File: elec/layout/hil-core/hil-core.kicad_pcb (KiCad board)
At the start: 4 copper layers, 113 parts, among them U4 10µH ±20%

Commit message: update LED gpio pin
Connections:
- net CC2 renamed B5
- net SW renamed buck_5v-cathode
- net controller.cm5-pins[47] renamed pins[47]
- net controller.cm5-pins[87] renamed controller.cm5-pins[89]
- net controller.cm5-pins[87]-1 renamed pins[87]
- net pins[23] renamed controller.cm5.hdi_b-pins[23]
- net pins[40] renamed controller.cm5.hdi_b-pins[40]
- net pins[53] renamed controller.cm5-pins[53]-1
- net pins[89] renamed controller.cm5-pins[89]-1
- net usb_connector.connector-B2 renamed B2
- net usbpd.usb_connector-B2 renamed SSTXP2
- C10 pad 1: hv-8 -> hv-7
- C11 pad 1: hv-8 -> hv-7
- C12 pad 1: hv -> hv-1
- C15 pad 1: hv-8 -> hv-7
- C16 pad 1: hv-1 -> hv
- C17 pad 1: hv-6 -> hv-9
- C18 pad 1: hv-6 -> hv-9
- C2 pad 1: hv-7 -> hv-4
- C20 pad 1: hv -> hv-1
- C21 pad 1: hv -> hv-1
- C26 pad 1: hv-2 -> hv-5
- C26 pad 2: gnd-1 -> gnd
- C27 pad 1: hv-2 -> hv-5
- C27 pad 2: gnd-1 -> gnd
- C28 pad 2: gnd-1 -> gnd
- C29 pad 2: gnd-1 -> gnd
- C3 pad 1: hv-7 -> hv-4
- C30 pad 1: hv -> hv-1
- C31 pad 1: hv -> hv-1
- C32 pad 1: hv -> hv-1
- C33 pad 1: hv -> hv-1
- C34 pad 1: hv -> hv-1
- C35 pad 1: hv -> hv-1
- C36 pad 1: hv -> hv-1
- C37 pad 1: hv -> hv-1
- C4 pad 1: hv-4 -> hv-6
- C40 pad 1: hv-8 -> hv-7
- C41 pad 1: hv-5 -> hv-2
- C42 pad 1: hv-5 -> hv-2
- C43 pad 1: hv-5 -> hv-2
- C44 pad 1: hv-5 -> hv-2
- C45 pad 1: hv-5 -> hv-2
- C5 pad 1: hv-4 -> hv-6
- C6 pad 1: hv-4 -> hv-6
- C9 pad 1: hv-4 -> hv-6
- CN1 pad 12: controller.cm5-line-4 -> controller.cm5-pins[23]
- CN1 pad 13: pins[25] -> controller.cm5-line-3
- CN1 pad 14: controller-line-3 -> controller-line
- CN1 pad 15: controller.cm5-line -> controller.cm5-line-5
- CN1 pad 18: controller-line-12 -> controller-line-4
- CN1 pad 19: controller-line-11 -> controller-line-29
- CN1 pad 2: controller-line-24 -> controller-line-9
- CN1 pad 20: controller-line-9 -> controller-line-8
- CN1 pad 22: controller-line-10 -> controller-line-24
- CN1 pad 23: line-4 -> line-10
- CN1 pad 24: controller.cm5-pins[47]-1 -> controller.cm5-line-1
- CN1 pad 25: line -> line-9
- CN1 pad 27: controller.cm5-line-1 -> controller.cm5-pins[53]
- CN1 pad 28: controller-line-26 -> controller-line-3
- CN1 pad 29: controller-line-16 -> controller-line-2
- CN1 pad 3: controller-line-4 -> controller-line-21
- CN1 pad 39: hv-9 -> hv-8
- CN1 pad 42: hv-9 -> hv-8
- CN1 pad 43: hv-9 -> hv-8
- CN1 pad 5: controller-line-2 -> controller-line-10
- CN1 pad 57: hv-8 -> hv-7
- CN1 pad 58: hv-8 -> hv-7
- CN1 pad 59: hv-8 -> hv-7
- CN1 pad 6: controller-line-21 -> controller-line-20
- CN1 pad 60: hv-8 -> hv-7
- CN1 pad 61: hv-8 -> hv-7
- CN1 pad 62: hv-8 -> hv-7
- CN1 pad 73: line-6 -> line-1
- CN1 pad 75: line-10 -> line-8
- CN1 pad 76: controller.cm5-line-3 -> controller.cm5-line-4
- CN1 pad 77: line-3 -> line-11
- CN1 pad 78: controller.cm5-line-5 -> controller.cm5-line
- CN1 pad 80: controller.cm5-line-2 -> controller.cm5-pins[40]
- CN1 pad 81: controller-line -> controller-line-6
- CN1 pad 82: controller-line-7 -> controller-line-31
- CN1 pad 83: controller-line-5 -> controller-line-19
- CN1 pad 85: controller-line-8 -> controller-line-7
- CN1 pad 86: line-9 -> line-6
- CN1 pad 88: pins[24] -> controller.cm5-line-2
- CN1 pad 92: controller-line-28 -> controller-line-14
- CN1 pad 93: controller-line-19 -> controller-line-25
- CN1 pad 95: controller-line-27 -> controller-line-1
- CN1 pad 96: controller-line-15 -> controller-line-11
- CN1 pad 99: controller-line-31 -> controller-line-12
- CN2 pad 15: controller-line-23 -> controller-line-26
- CN2 pad 17: controller-line-17 -> controller-line-27
- CN2 pad 18: controller-line-20 -> controller-line-22
- CN2 pad 20: controller-line-1 -> controller-line-18
- CN2 pad 21: controller-line-6 -> controller-line-23
- CN2 pad 65: controller-line-22 -> controller-line-17
- CN2 pad 66: controller-line-25 -> controller-line-13
- CN2 pad 68: controller-line-13 -> controller-line-16
- CN2 pad 69: controller-line-18 -> controller-line-5
- CN2 pad 71: controller-line-29 -> controller-line-15
- CN2 pad 72: controller-line-14 -> controller-line-28
- CN2 pad 98: line-2 -> line
- CN2 pad 99: line-1 -> line-4
- D1 pad 1: hv-4 -> hv-6
- D10 pad 2: usb_hub-line-2 -> usb_hub-line
- D10 pad 3: usb_hub-line-1 -> usb_hub-line-4
- D10 pad 4: hv-5 -> hv-2
- D11 pad 2: usb_hub-line -> usb_hub-line-1
- D11 pad 3: usb_hub-line-4 -> usb_hub-line-2
- D11 pad 4: hv-5 -> hv-2
- D12 pad 2: line-8 -> line-7
- D12 pad 3: line-7 -> line-3
- D12 pad 4: hv-5 -> hv-2
- D2 pad 1: controller.cm5-cathode-1 -> controller.cm5-cathode
- D2 pad 2: hv-9 -> hv-8
- D3 pad 1: controller.cm5-cathode -> controller.cm5-cathode-1
- D3 pad 2: hv-9 -> hv-8
- D4 pad 1: usbpd-line-5 -> usbpd-line-2
- D4 pad 2: usbpd-line-3 -> usbpd-line-4
- D6 pad 1: hv-7 -> hv-4
- D7 pad 1: gnd-1 -> gnd
- D7 pad 2: line-11 -> line-5
- D7 pad 3: line-5 -> line-2
- D8 pad 2: line-11 -> line-5
- D8 pad 3: line-5 -> line-2
- D8 pad 4: hv-5 -> hv-2
- D9 pad 2: line-1 -> line-4
- D9 pad 3: line-2 -> line
- D9 pad 4: hv-5 -> hv-2
- L1 pad 1: hv-7 -> hv-4
- OLED1 pad 10: line-3 -> line-11
- OLED1 pad 11: line-4 -> line-10
- OLED1 pad 14: hv-6 -> hv-9
- OLED1 pad 5: hv-1 -> hv
- OLED1 pad 8: hv -> hv-1
- Q1 pad 5: hv-7 -> hv-4
- Q1 pad 6: hv-7 -> hv-4
- Q1 pad 7: hv-7 -> hv-4
- Q1 pad 8: hv-7 -> hv-4
- Q1 pad 9: hv-7 -> hv-4
- R10 pad 1: hv-9 -> hv-8
- R10 pad 2: controller.rj45-anode -> controller.rj45-anode-1
- R12 pad 1: hv -> hv-1
- R15 pad 1: hv-1 -> hv
- R17 pad 1: usbpd-line-4 -> usbpd-line-1
- R18 pad 1: usbpd-line -> usbpd-line-3
- R2 pad 1: hv-4 -> hv-6
- R20 pad 2: hv-7 -> hv-4
- R23 pad 2: gnd-1 -> gnd
- R25 pad 1: usb_hub.hub-line -> usb_hub.hub-line-1
- R26 pad 1: usb_hub.hub-line-1 -> usb_hub.hub-line
- R6 pad 1: hv-8 -> hv-7
- R7 pad 1: controller.cm5-cathode-1 -> controller.cm5-cathode
- R8 pad 1: controller.cm5-cathode -> controller.cm5-cathode-1
- R9 pad 1: hv-9 -> hv-8
- R9 pad 2: controller.rj45-anode-1 -> controller.rj45-anode
- RJ1 pad 11: controller.rj45-anode-1 -> controller.rj45-anode
- RJ1 pad 12: controller-line-19 -> controller-line-25
- RJ1 pad 13: controller-line-28 -> controller-line-14
- RJ1 pad 14: controller.rj45-anode -> controller.rj45-anode-1
- RJ1 pad P2: controller-line-21 -> controller-line-20
- RJ1 pad P3: controller-line-2 -> controller-line-10
- RJ1 pad P4: controller-line-24 -> controller-line-9
- RJ1 pad P5: controller-line-27 -> controller-line-1
- RJ1 pad P6: controller-line-15 -> controller-line-11
- RJ1 pad P7: controller-line-4 -> controller-line-21
- RJ1 pad P8: controller-line-31 -> controller-line-12
- U1 pad 2: hv-7 -> hv-4
- U1 pad 3: hv-7 -> hv-4
- U10 pad 1: hv-8 -> hv-7
- U10 pad 3: hv-8 -> hv-7
- U10 pad 5: hv -> hv-1
- U11 pad 1: hv-8 -> hv-7
- U11 pad 3: hv-8 -> hv-7
- U11 pad 5: hv-1 -> hv
- U12 pad 1: usbpd-line-5 -> usbpd-line-2
- U12 pad 2: usbpd-line-5 -> usbpd-line-2
- U12 pad 4: usbpd-line-3 -> usbpd-line-4
- U12 pad 5: usbpd-line-3 -> usbpd-line-4
- U12 pad 7: usbpd-line-4 -> usbpd-line-1
- U12 pad 8: usbpd-line -> usbpd-line-3
- U13 pad 1: usb_uart-line-3 -> usb_uart-line
- U13 pad 2: usb_uart-line -> usb_uart-line-3
- U13 pad 23: line -> line-9
- U13 pad 24: line-9 -> line-6
- U13 pad 25: line-6 -> line-1
- U13 pad 26: line-10 -> line-8
- U13 pad 29: gnd-1 -> gnd
- U13 pad 3: gnd-1 -> gnd
- U13 pad 4: line-5 -> line-2
- U13 pad 5: line-11 -> line-5
- U13 pad 7: hv-2 -> hv-5
- U14 pad 1: line-11 -> line-5
- U14 pad 10: hv -> hv-1
- U14 pad 15: hv -> hv-1
- U14 pad 2: line-5 -> line-2
- U14 pad 22: usb_hub.hub-line-1 -> usb_hub.hub-line
- U14 pad 23: hv -> hv-1
- U14 pad 24: usb_hub.hub-line -> usb_hub.hub-line-1
- U14 pad 27: hv -> hv-1
- U14 pad 29: hv -> hv-1
- U14 pad 3: line-1 -> line-4
- U14 pad 30: line-8 -> line-7
- U14 pad 31: line-7 -> line-3
- U14 pad 36: hv -> hv-1
- U14 pad 4: line-2 -> line
- U14 pad 5: hv -> hv-1
- U14 pad 6: usb_hub-line-2 -> usb_hub-line
- U14 pad 7: usb_hub-line-1 -> usb_hub-line-4
- U14 pad 8: usb_hub-line -> usb_hub-line-1
- U14 pad 9: usb_hub-line-4 -> usb_hub-line-2
- U15 pad 1: hv-8 -> hv-7
- U15 pad 6: hv-5 -> hv-2
- U3 pad 4: hv-4 -> hv-6
- U3 pad 5: hv-4 -> hv-6
- U4 pad 2: hv-8 -> hv-7
- U5 pad 5: hv-9 -> hv-8
- USB1 pad A5: usbpd-line-5 -> usbpd-line-2
- USB1 pad A6: usbpd-line-1 -> usbpd-line
- USB1 pad A7: usbpd-line-2 -> usbpd-line-5
- USB1 pad B5: usbpd-line-3 -> usbpd-line-4
- USB1 pad B6: usbpd-line-1 -> usbpd-line
- USB1 pad B7: usbpd-line-2 -> usbpd-line-5
- USB2 pad A6: line-7 -> line-3
- USB2 pad A7: line-8 -> line-7
- USB2 pad B6: line-7 -> line-3
- USB2 pad B7: line-8 -> line-7
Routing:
- net (no net): track 207.6 -> 330.8 mm, vias 8 -> 74
- net gnd-1: track 123.1 -> 0.00 mm, vias 66 -> 0
- net line-8: track 58.7 -> 0.00 mm, vias 3 -> 0
- net line-3: track 0.00 -> 53.8 mm, vias 0 -> 2
- net line-4: track 0.00 -> 38.7 mm, vias 0 -> 2
- net line-1: track 38.7 -> 0.00 mm, vias 2 -> 0
- net line: track 0.00 -> 38.1 mm, vias 0 -> 2
- net hv-5: track 40.8 -> 3.36 mm, vias 6 -> 0
- net hv-2: track 3.36 -> 40.8 mm, vias 0 -> 6
- net controller-line-28: track 29.5 -> 0.00 mm, vias 1 -> 0
- net controller-line-14: track 0.00 -> 29.5 mm, vias 0 -> 1
- net controller-line-25: track 0.00 -> 24.6 mm, vias 0 -> 1
- net controller-line-19: track 24.6 -> 0.00 mm, vias 1 -> 0
- net line-2: track 38.1 -> 14.9 mm
- net controller-line-2: track 19.6 -> 0.00 mm, vias 1 -> 0
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- added copper zone on F.Cu, net hv-6
- removed copper zone on F.Cu, net hv-8

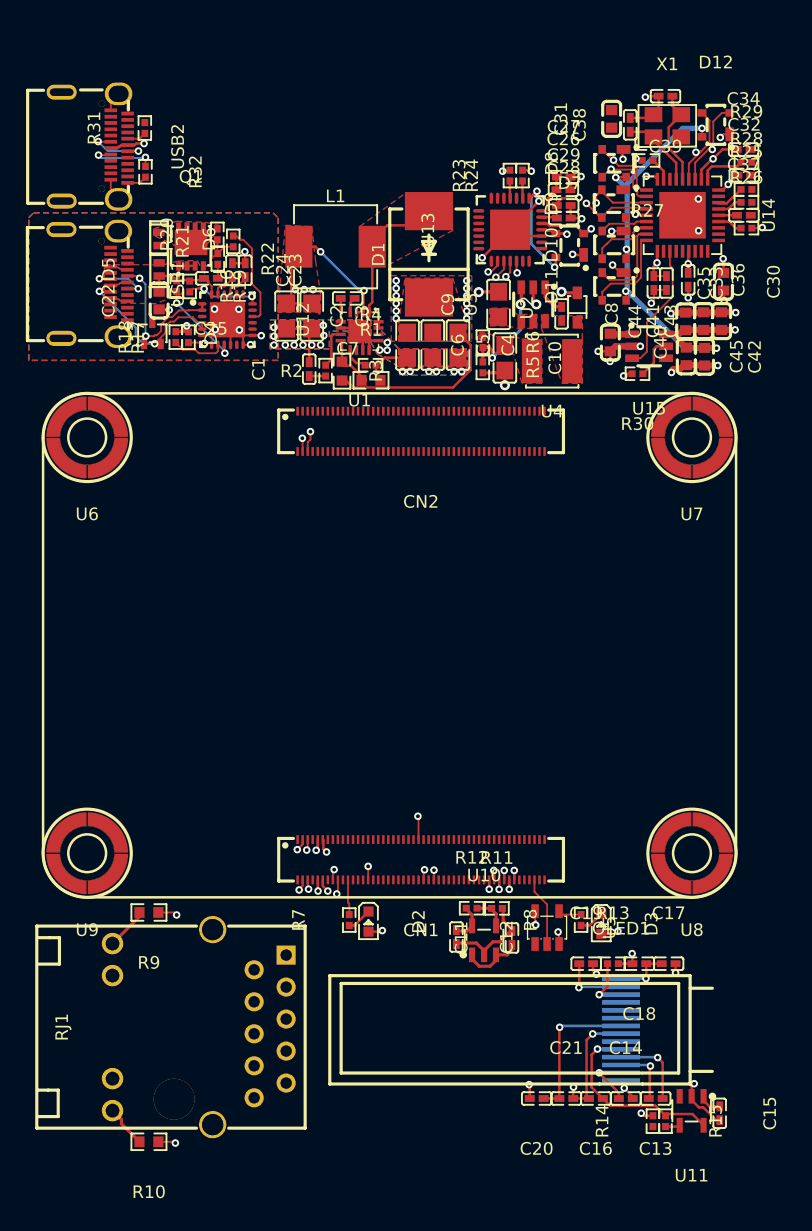
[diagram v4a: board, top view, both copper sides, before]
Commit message: add power button and boot button, fix CAN layout
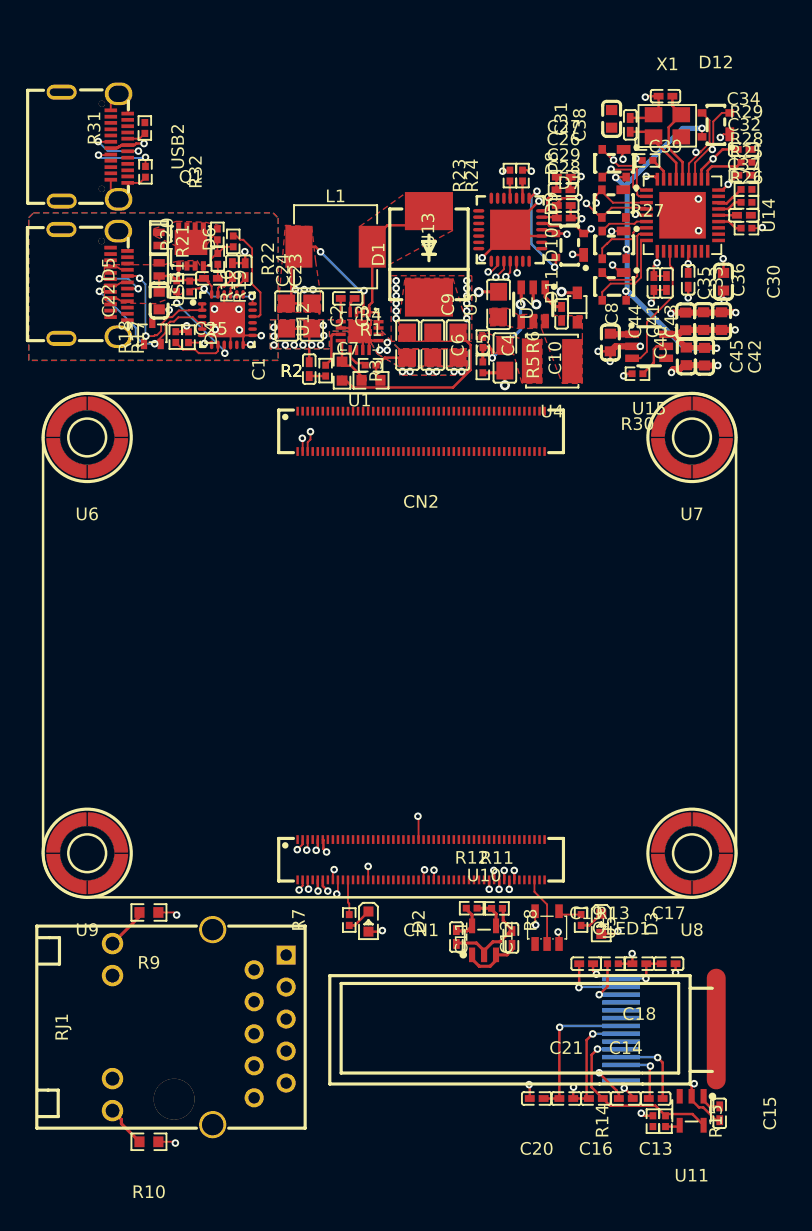
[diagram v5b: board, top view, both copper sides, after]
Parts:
- R11: value 10kΩ ±1% 62.5mW -> 5.6kΩ ±1% 62.5mW
- R6: value 10kΩ ±1% 62.5mW -> 47kΩ ±1% 62.5mW
- R7, R8: value 10kΩ ±1% 62.5mW -> 2kΩ ±1% 62.5mW
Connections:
- net B2 renamed usb_connector.connector-B2
- net SSTXP2 renamed usbpd.usb_connector-B2
- net buck_5v-cathode renamed SW
- net controller.cm5-pins[53]-1 renamed pins[53]
- net controller.cm5-pins[89] renamed controller.cm5-pins[87]
- net controller.cm5-pins[89]-1 renamed pins[89]
- net controller.cm5.hdi_b-pins[23] renamed pins[23]
- net controller.cm5.hdi_b-pins[26] renamed pins[26]
- net pins[44] renamed controller.cm5-pins[44]-1
- net pins[48] renamed controller.cm5-pins[48]-1
- net pins[87] renamed controller.cm5-pins[87]-1
- net usb_connector.connector-A2 renamed SSTXP1
- net usb_connector.connector-A3 renamed SSTXN1
- net usb_connector.connector-A8 renamed SBU1
- net usb_connector.connector-B10 renamed SSRXN1
- net usb_connector.connector-B11 renamed SSRXP1
- net usbpd.usb_connector-A2 renamed A2
- net usbpd.usb_connector-A3 renamed A3
- net usbpd.usb_connector-A8 renamed A8
- net usbpd.usb_connector-B10 renamed B10
- net usbpd.usb_connector-B11 renamed B11
- C10 pad 1: hv-7 -> hv-8
- C11 pad 1: hv-7 -> hv-8
- C12 pad 1: hv-1 -> hv
- C15 pad 1: hv-7 -> hv-8
- C16 pad 1: hv -> hv-1
- C17 pad 1: hv-9 -> hv-4
- C18 pad 1: hv-9 -> hv-4
- C2 pad 1: hv-4 -> hv-2
- C20 pad 1: hv-1 -> hv
- C21 pad 1: hv-1 -> hv
- C26 pad 1: hv-5 -> hv-6
- C27 pad 1: hv-5 -> hv-6
- C28 pad 1: hv-3 -> hv-7
- C29 pad 1: hv-3 -> hv-7
- C3 pad 1: hv-4 -> hv-2
- C30 pad 1: hv-1 -> hv
- C31 pad 1: hv-1 -> hv
- C32 pad 1: hv-1 -> hv
- C33 pad 1: hv-1 -> hv
- C34 pad 1: hv-1 -> hv
- C35 pad 1: hv-1 -> hv
- C36 pad 1: hv-1 -> hv
- C37 pad 1: hv-1 -> hv
- C4 pad 1: hv-6 -> hv-9
- C40 pad 1: hv-7 -> hv-8
- C41 pad 1: hv-2 -> hv-3
- C42 pad 1: hv-2 -> hv-3
- C43 pad 1: hv-2 -> hv-3
- C44 pad 1: hv-2 -> hv-3
- C45 pad 1: hv-2 -> hv-3
- C5 pad 1: hv-6 -> hv-9
- C6 pad 1: hv-6 -> hv-9
- C9 pad 1: hv-6 -> hv-9
- CN1 pad 12: controller.cm5-pins[23] -> controller.cm5-line-3
- CN1 pad 13: controller.cm5-line-3 -> controller.cm5-line-4
- CN1 pad 14: controller-line -> controller-line-8
- CN1 pad 15: controller.cm5-line-5 -> controller-line-27
- CN1 pad 18: controller-line-4 -> controller-line-18
- CN1 pad 19: controller-line-29 -> controller-line-13
- CN1 pad 2: controller-line-9 -> controller-line-3
- CN1 pad 20: controller-line-8 -> controller-line-7
- CN1 pad 22: controller-line-24 -> controller-line-17
- CN1 pad 23: line-10 -> line-11
- CN1 pad 24: controller.cm5-line-1 -> controller.cm5-line
- CN1 pad 25: line-9 -> line-6
- CN1 pad 27: controller.cm5-pins[53] -> controller.cm5-line-5
- CN1 pad 28: controller-line-3 -> controller-line-6
- CN1 pad 3: controller-line-21 -> controller-line-30
- CN1 pad 39: hv-8 -> hv-5
- CN1 pad 42: hv-8 -> hv-5
- CN1 pad 43: hv-8 -> hv-5
- CN1 pad 5: controller-line-10 -> controller-line-25
- CN1 pad 57: hv-7 -> hv-8
- CN1 pad 58: hv-7 -> hv-8
- CN1 pad 59: hv-7 -> hv-8
- CN1 pad 6: controller-line-20 -> controller-line-16
- CN1 pad 60: hv-7 -> hv-8
- CN1 pad 61: hv-7 -> hv-8
- CN1 pad 62: hv-7 -> hv-8
- CN1 pad 73: line-1 -> line-4
- CN1 pad 75: line-8 -> line-2
- CN1 pad 76: controller.cm5-line-4 -> controller.cm5-pins[48]
- CN1 pad 77: line-11 -> line-10
- CN1 pad 78: controller.cm5-line -> controller.cm5-pins[44]
- CN1 pad 81: controller-line-6 -> controller-line-23
- CN1 pad 82: controller-line-31 -> controller-line-4
- CN1 pad 83: controller-line-19 -> controller-line-26
- CN1 pad 85: controller-line-7 -> controller-line-19
- CN1 pad 86: line-6 -> line-7
- CN1 pad 87: controller.cm5-pins[26] -> controller-line-22
- CN1 pad 88: controller.cm5-line-2 -> controller.cm5-line-1
- CN1 pad 92: controller-line-14 -> controller-line-1
- CN1 pad 93: controller-line-25 -> controller-line-15
- CN1 pad 95: controller-line-1 -> controller-line
- CN1 pad 96: controller-line-11 -> controller-line-24
- CN1 pad 98: controller-line-30 -> controller-line-28
- CN1 pad 99: controller-line-12 -> controller-line-32
- CN2 pad 15: controller-line-26 -> controller-line-10
- CN2 pad 17: controller-line-27 -> controller-line-20
- CN2 pad 18: controller-line-22 -> controller-line-31
- CN2 pad 20: controller-line-18 -> controller-line-12
- CN2 pad 21: controller-line-23 -> controller-line-14
- CN2 pad 65: controller-line-17 -> controller-line-11
- CN2 pad 66: controller-line-13 -> controller-line-5
- CN2 pad 68: controller-line-16 -> controller-line-29
- CN2 pad 69: controller-line-5 -> controller-line-9
- CN2 pad 71: controller-line-15 -> controller-line-21
- CN2 pad 72: controller-line-28 -> controller-line-33
- CN2 pad 98: line -> line-1
- CN2 pad 99: line-4 -> line-3
- D1 pad 1: hv-6 -> hv-9
- D10 pad 2: usb_hub-line -> usb_hub-line-2
- D10 pad 4: hv-2 -> hv-3
- D11 pad 2: usb_hub-line-1 -> usb_hub-line
- D11 pad 3: usb_hub-line-2 -> usb_hub-line-1
- D11 pad 4: hv-2 -> hv-3
- D12 pad 2: line-7 -> line-5
- D12 pad 3: line-3 -> line-9
- D12 pad 4: hv-2 -> hv-3
- D2 pad 1: controller.cm5-cathode -> controller.cm5-cathode-1
- D2 pad 2: hv-8 -> hv-5
- D3 pad 1: controller.cm5-cathode-1 -> controller.cm5-cathode
- D3 pad 2: hv-8 -> hv-5
- D4 pad 1: usbpd-line-2 -> usbpd-line-5
- D4 pad 2: usbpd-line-4 -> usbpd-line-2
- D6 pad 1: hv-4 -> hv-2
- D7 pad 2: line-5 -> line-8
- D7 pad 3: line-2 -> line
- D8 pad 2: line-5 -> line-8
- D8 pad 3: line-2 -> line
- D8 pad 4: hv-2 -> hv-3
- D9 pad 2: line-4 -> line-3
- D9 pad 3: line -> line-1
- D9 pad 4: hv-2 -> hv-3
- L1 pad 1: hv-4 -> hv-2
- OLED1 pad 10: line-11 -> line-10
- OLED1 pad 11: line-10 -> line-11
- OLED1 pad 14: hv-9 -> hv-4
- OLED1 pad 5: hv -> hv-1
- OLED1 pad 8: hv-1 -> hv
- Q1 pad 5: hv-4 -> hv-2
- Q1 pad 6: hv-4 -> hv-2
- Q1 pad 7: hv-4 -> hv-2
- Q1 pad 8: hv-4 -> hv-2
- Q1 pad 9: hv-4 -> hv-2
- R10 pad 1: hv-8 -> hv-5
- R12 pad 1: hv-1 -> hv
- R15 pad 1: hv -> hv-1
- R18 pad 1: usbpd-line-3 -> usbpd-line-4
- R2 pad 1: hv-6 -> hv-9
- R20 pad 2: hv-4 -> hv-2
- R24 pad 2: hv-3 -> hv-7
- R25 pad 1: usb_hub.hub-line-1 -> usb_hub.hub-line
- R26 pad 1: usb_hub.hub-line -> usb_hub.hub-line-1
- R6 pad 1: hv-7 -> hv-8
- R7 pad 1: controller.cm5-cathode -> controller.cm5-cathode-1
- R8 pad 1: controller.cm5-cathode-1 -> controller.cm5-cathode
- R8 pad 2: Y -> controller.cm5-line-2
- R9 pad 1: hv-8 -> hv-5
- RJ1 pad 12: controller-line-25 -> controller-line-15
- RJ1 pad 13: controller-line-14 -> controller-line-1
- RJ1 pad P2: controller-line-20 -> controller-line-16
- RJ1 pad P3: controller-line-10 -> controller-line-25
- RJ1 pad P4: controller-line-9 -> controller-line-3
- RJ1 pad P5: controller-line-1 -> controller-line
- RJ1 pad P6: controller-line-11 -> controller-line-24
- RJ1 pad P7: controller-line-21 -> controller-line-30
- RJ1 pad P8: controller-line-12 -> controller-line-32
- RJ1 pad P9: controller-line-30 -> controller-line-28
- U1 pad 2: hv-4 -> hv-2
- U1 pad 3: hv-4 -> hv-2
- U10 pad 1: hv-7 -> hv-8
- U10 pad 3: hv-7 -> hv-8
- U10 pad 5: hv-1 -> hv
- U11 pad 1: hv-7 -> hv-8
- U11 pad 3: hv-7 -> hv-8
- U11 pad 5: hv -> hv-1
- U12 pad 1: usbpd-line-2 -> usbpd-line-5
- U12 pad 2: usbpd-line-2 -> usbpd-line-5
- U12 pad 4: usbpd-line-4 -> usbpd-line-2
- U12 pad 5: usbpd-line-4 -> usbpd-line-2
- U12 pad 8: usbpd-line-3 -> usbpd-line-4
- U13 pad 1: usb_uart-line -> usb_uart-line-2
- U13 pad 2: usb_uart-line-3 -> usb_uart-line
- U13 pad 23: line-9 -> line-6
- U13 pad 24: line-6 -> line-7
- U13 pad 25: line-1 -> line-4
- U13 pad 26: line-8 -> line-2
- U13 pad 27: usb_uart-line-1 -> usb_uart-line-3
- U13 pad 28: usb_uart-line-2 -> usb_uart-line-1
- U13 pad 4: line-2 -> line
- U13 pad 5: line-5 -> line-8
- U13 pad 6: hv-3 -> hv-7
- U13 pad 7: hv-5 -> hv-6
- U14 pad 1: line-5 -> line-8
- U14 pad 10: hv-1 -> hv
- U14 pad 15: hv-1 -> hv
- U14 pad 2: line-2 -> line
- U14 pad 22: usb_hub.hub-line -> usb_hub.hub-line-1
- U14 pad 23: hv-1 -> hv
- U14 pad 24: usb_hub.hub-line-1 -> usb_hub.hub-line
- U14 pad 27: hv-1 -> hv
- U14 pad 29: hv-1 -> hv
- U14 pad 3: line-4 -> line-3
- U14 pad 30: line-7 -> line-5
- U14 pad 31: line-3 -> line-9
- U14 pad 36: hv-1 -> hv
- U14 pad 4: line -> line-1
- U14 pad 5: hv-1 -> hv
- U14 pad 6: usb_hub-line -> usb_hub-line-2
- U14 pad 8: usb_hub-line-1 -> usb_hub-line
- U14 pad 9: usb_hub-line-2 -> usb_hub-line-1
- U15 pad 1: hv-7 -> hv-8
- U15 pad 6: hv-2 -> hv-3
- U3 pad 4: hv-6 -> hv-9
- U3 pad 5: hv-6 -> hv-9
- U4 pad 2: hv-7 -> hv-8
- U5 pad 4: Y -> controller.cm5-line-2
- U5 pad 5: hv-8 -> hv-5
- USB1 pad A5: usbpd-line-2 -> usbpd-line-5
- USB1 pad A7: usbpd-line-5 -> usbpd-line-3
- USB1 pad B5: usbpd-line-4 -> usbpd-line-2
- USB1 pad B7: usbpd-line-5 -> usbpd-line-3
- USB2 pad A6: line-3 -> line-9
- USB2 pad A7: line-7 -> line-5
- USB2 pad B6: line-3 -> line-9
- USB2 pad B7: line-7 -> line-5
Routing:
- net (no net): track 330.8 -> 207.6 mm, vias 74 -> 8
- net gnd: track 0.00 -> 123.1 mm, vias 0 -> 66
- net line-7: track 58.7 -> 0.00 mm, vias 3 -> 0
- net line-9: track 0.00 -> 53.8 mm, vias 0 -> 2
- net line-5: track 16.9 -> 58.7 mm, vias 2 -> 3
- net line-4: track 38.7 -> 0.00 mm, vias 2 -> 0
- net line-1: track 0.00 -> 38.1 mm, vias 0 -> 2
- net hv-3: track 6.02 -> 40.8 mm, vias 2 -> 6
- net controller-line-14: track 29.5 -> 0.00 mm, vias 1 -> 0
- net controller-line-15: track 0.00 -> 24.6 mm, vias 0 -> 1
- net hv-2: track 40.8 -> 17.0 mm, vias 6 -> 5
- net line: track 38.1 -> 14.9 mm
- net controller-line-10: track 19.6 -> 0.00 mm, vias 1 -> 0
- net controller-line-21: track 18.8 -> 0.00 mm, vias 1 -> 0
- net controller-line-32: track 0.00 -> 18.6 mm, vias 0 -> 1
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- added copper zone on F.Cu, net hv-2
- added copper zone on F.Cu, net hv-8
- added copper zone on F.Cu, net hv-9
- removed copper zone on F.Cu, net hv-4
- removed copper zone on F.Cu, net hv-6
- removed copper zone on F.Cu, net hv-7
